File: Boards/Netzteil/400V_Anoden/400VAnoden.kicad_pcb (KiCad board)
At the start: 2 copper layers, 160 x 100 mm, 43 parts, among them P1 Drossel, P2 320V_AC, P3 CONN_3, P4 133V_AC, P5 CONN_3, Q1 2SC2979

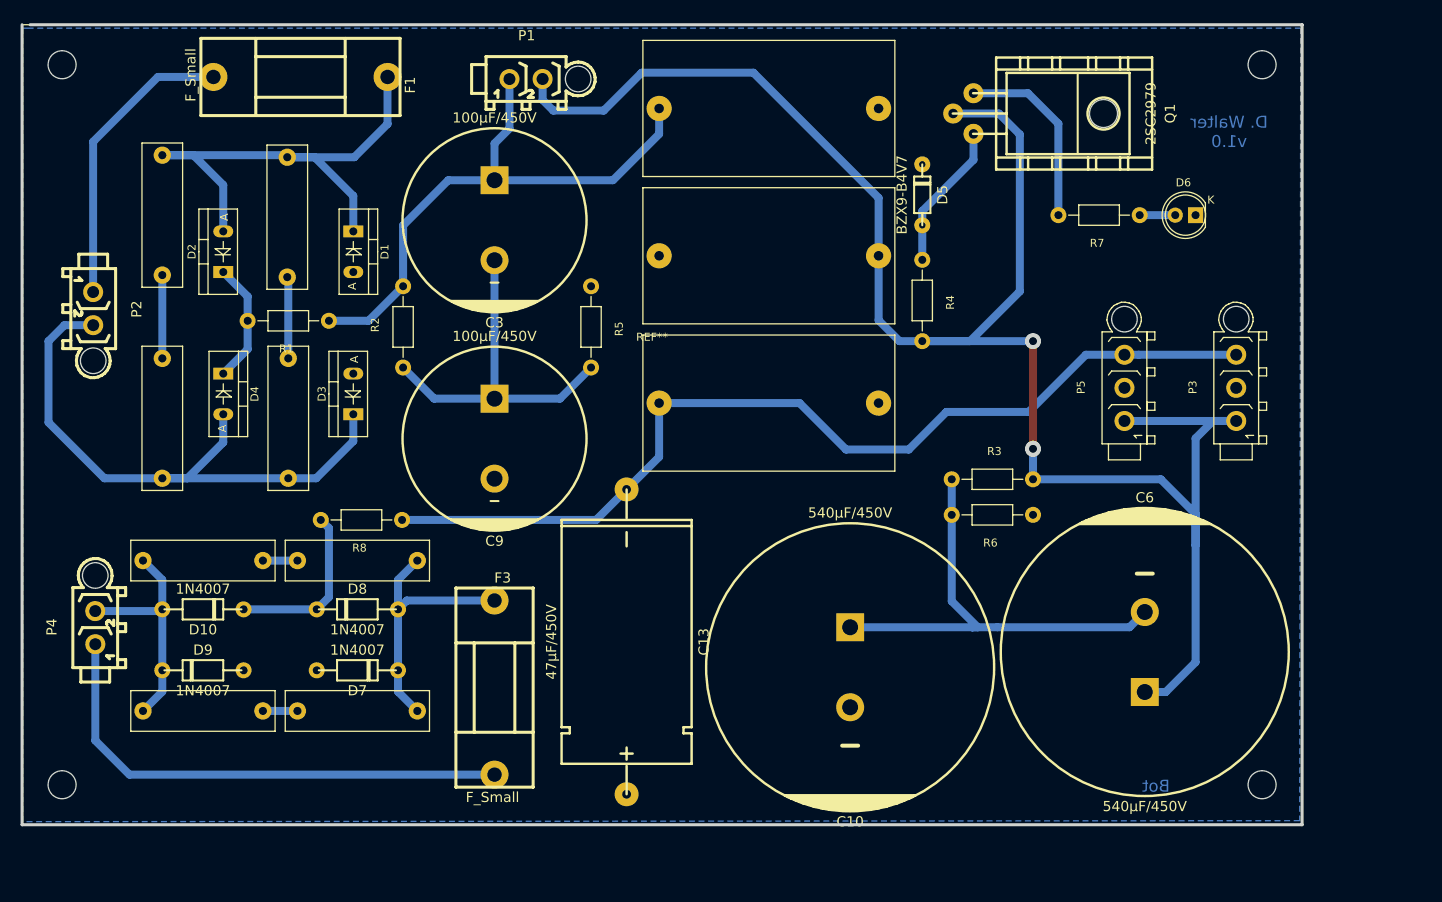
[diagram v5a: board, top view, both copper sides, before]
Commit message: Converted to Kicad 5.1 and Layout changes
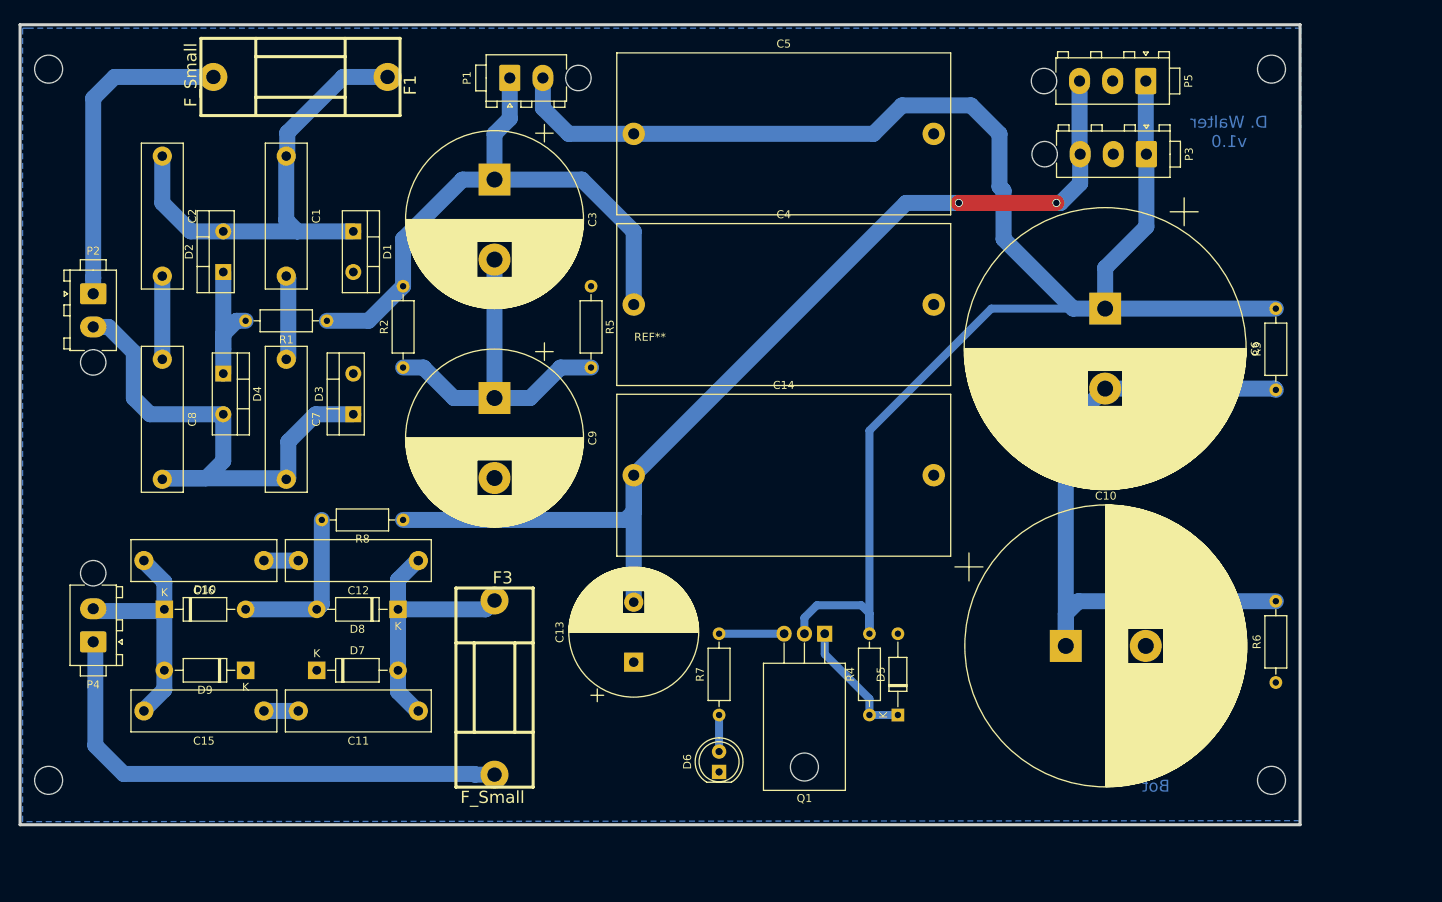
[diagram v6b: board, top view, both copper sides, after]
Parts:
- C1, C11, C12, C15, C16, C2, C7, C8: footprint Capacitor-Wima-FKP1-1600v:Capacitor-Wima-FKP1-1600v-R15B5 -> Capacitor_THT:C_Rect_L18.0mm_W5.0mm_P15.00mm_FKS3_FKP3
- C10, C6: footprint w_capacitors:CP_35x40mm -> Capacitor_THT:CP_Radial_D35.0mm_P10.00mm_SnapIn
- C13: footprint w_capacitors:CPA_16x31MM -> Capacitor_THT:CP_Radial_D16.0mm_P7.50mm
- C14, C4, C5: footprint Capacitor-Wima-MKP10-630v:Capacitor-Wima-MKP10-630v-R27K5B17 -> Capacitor_THT:C_Rect_L41.5mm_W20.0mm_P37.50mm_MKS4
- C3, C9: footprint w_capacitors:CP_22x25mm -> Capacitor_THT:CP_Radial_D22.0mm_P10.00mm_SnapIn
- D1, D2, D3, D4: footprint Diodes_ThroughHole:Diode_TO-220_Vertical -> Package_TO_SOT_THT:TO-220-2_Vertical
- D10, D7, D8, D9: footprint w_pth_diodes:diode_do41 -> Diode_THT:D_DO-41_SOD81_P10.16mm_Horizontal
- D5: footprint w_pth_diodes:diode_do35 -> Diode_THT:D_DO-35_SOD27_P10.16mm_Horizontal
- D6: footprint LEDs:LED-5MM -> LED_THT:LED_D5.0mm
- P1, P2, P4: footprint MiniUniversalMate-N-LokSockets_13Aug2012:MiniUniversalMate-N-LokSocket_2PinVertical_12Aug2012 -> Connector_TE-Connectivity:TE_MATE-N-LOK_1-770866-x_1x02_P4.14mm_Vertical
- P3, P5: footprint Connectors_Mini-Universal:MiniUniversalMate-N-LokSocket_3PinVertical -> Connector_TE-Connectivity:TE_MATE-N-LOK_1-770870-x_1x03_P4.14mm_Vertical
- Q1: footprint w_to:to220-horiz_5770 -> Package_TO_SOT_THT:TO-220-3_Horizontal_TabDown
- R1, R2, R3, R4, R5, R6, R7, R8: footprint Resistors_ThroughHole:Resistor_Horizontal_RM10mm -> Resistor_THT:R_Axial_DIN0207_L6.3mm_D2.5mm_P10.16mm_Horizontal
- moved D6 91.6 mm to (124.0, 120.4), turned to 90 degrees
- moved R7 78.5 mm to (124.0, 113.3), turned to 90 degrees
- moved Q1 70.4 mm to (137.2, 103.1), turned to 180 degrees
- moved D5 65.1 mm to (146.3, 113.3)
- moved R4 52.2 mm to (142.7, 113.3), turned to 90 degrees
- moved C6 43.2 mm to (172.2, 62.5), turned to 270 degrees
- moved R6 41.2 mm to (193.5, 109.2), turned to 90 degrees
- moved P5 38.4 mm to (177.3, 34.0), turned to 270 degrees
- moved R3 37.2 mm to (193.5, 72.6), turned to 90 degrees
- moved P3 31.3 mm to (177.4, 43.2), turned to 270 degrees
- moved C4 29.8 mm to (113.3, 62.0)
- moved C10 27.1 mm to (167.3, 104.6), turned to 0 degrees
- moved C5 22.8 mm to (113.3, 40.6), turned to 0 degrees
- moved C14 19.1 mm to (113.3, 83.3)
- moved C1 7.64 mm to (69.8, 43.4)
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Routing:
- net Net-(C10-Pad1): track 58.3 -> 86.5 mm
- net Net-(Q1-Pad3): track 23.6 -> 8.13 mm
- net /-180V_DC: track 121.6 -> 133.4 mm, vias 0 -> 2
- net /+450V_DC: track 232.2 -> 221.6 mm, vias 2 -> 0
- net Net-(C7-Pad2): track 76.9 -> 68.6 mm
- net Net-(C1-Pad1): track 66.4 -> 59.7 mm
- net Net-(F1-Pad1): track 37.2 -> 40.4 mm
- net Net-(D2-Pad1): track 15.2 -> 18.1 mm
- net Net-(D5-Pad1): track 18.4 -> 16.0 mm
- net Net-(C3-Pad1): track 72.6 -> 74.3 mm
- net Net-(D10-Pad2): track 21.4 -> 20.3 mm
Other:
- outline, holes or cut-outs redrawn

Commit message: Minor Layout changes
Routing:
- net /+450V_DC: track 221.6 -> 222.5 mm
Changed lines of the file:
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@@
     (thickness 1.6)
     (drawings 2)
-    (tracks 135)
+    (tracks 133)
     (zones 0)
     (modules 43)
@@
   )
   (setup
-    (last_trace_width 1)
+    (last_trace_width 0.5)
     (user_trace_width 0.5)
     (user_trace_width 1)
@@
   (segment (start 134.62 101.124) (end 136.176 99.568) (width 1) (layer B.Cu) (net 20))
   (segment (start 168.212 62.484) (end 172.212 62.484) (width 2) (layer B.Cu) (net 20))
-  (segment (start 143.256 40.64) (end 146.812 37.084) (width 2) (layer B.Cu) (net 20))
+  (segment (start 143.256 40.64) (end 147.828 36.068) (width 2) (layer B.Cu) (net 20))
   (segment (start 113.284 40.64) (end 143.256 40.64) (width 2) (layer B.Cu) (net 20))
-  (segment (start 146.812 37.084) (end 155.448 37.084) (width 2) (layer B.Cu) (net 20))
-  (segment (start 159.512 53.784) (end 168.212 62.484) (width 2) (layer B.Cu) (net 20))
-  (segment (start 155.448 37.084) (end 159.004 40.64) (width 2) (layer B.Cu) (net 20))
-  (segment (start 159.512 47.752) (end 159.512 53.784) (width 2) (layer B.Cu) (net 20))
-  (segment (start 159.004 40.64) (end 159.004 47.244) (width 2) (layer B.Cu) (net 20))
-  (segment (start 159.004 47.244) (end 159.512 47.752) (width 2) (layer B.Cu) (net 20))
+  (segment (start 147.828 36.068) (end 154.432 36.068) (width 2) (layer B.Cu) (net 20))
+  (segment (start 154.432 36.068) (end 159.004 40.64) (width 2) (layer B.Cu) (net 20))
+  (segment (start 159.004 40.64) (end 159.004 53.276) (width 2) (layer B.Cu) (net 20))
+  (segment (start 159.004 53.276) (end 168.212 62.484) (width 2) (layer B.Cu) (net 20))
   (segment (start 113.284 99.18) (end 113.284 83.312) (width 2) (layer B.Cu) (net 21))
   (segment (start 113.284 87.884) (end 113.284 83.312) (width 2) (layer B.Cu) (net 21))

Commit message: Layout changes, Supply connector changes, Mounting holes
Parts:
- added P6: Trafo, Connector_TE-Connectivity:TE_MATE-N-LOK_1-770866-x_1x02_P4.14mm_Vertical, F.Cu at (158.8, 34.2)
- added P7: Trafo, Connector_TE-Connectivity:TE_MATE-N-LOK_1-770866-x_1x02_P4.14mm_Vertical, F.Cu at (167.9, 34.2)
- added REF**: Symbol_HighVoltage_Type2_CopperTop_VerySmall, Symbol:Symbol_HighVoltage_Type2_CopperTop_VerySmall, B.Cu at (176.0, 84.8)
- P3, P5: value CONN_3 -> Stabi
- moved P3 12.6 mm to (186.2, 34.2), turned to 0 degrees
- moved C6 4.06 mm to (172.2, 66.5)
- moved R6 3.84 mm to (193.0, 113.0)
- moved R3 3.82 mm to (193.3, 76.5)
- moved C10 3.30 mm to (167.3, 108.0)
- moved P5 0.28 mm to (177.0, 34.2), turned to 0 degrees
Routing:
- net /+450V_DC: track 222.5 -> 234.6 mm
- net /-180V_DC: track 133.4 -> 144.9 mm
- net Net-(C10-Pad1): track 86.5 -> 84.5 mm
- net Net-(D5-Pad1): track 16.0 -> 17.0 mm
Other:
- board text added: "HIGH VOLTAGE"
- board text added: "High Voltage present when lit!"
